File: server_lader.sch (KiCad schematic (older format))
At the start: 20 parts

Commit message: update
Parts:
- removed D? (x2): DIODE, symbol DIODE
- removed U?: LM7909CT, TO-220, symbol LM7909CT
- removed U?: LM7809CT, TO-220, symbol LM7809CT
- added C? (x2): 10nF, symbol C
- added C? (x2): 10uF, symbol C
- added C? (x3): 100nF, symbol C
- added C?: 1uF, symbol C
- added DISP?: EA_DOG-M, symbol EA_DOG-M
- added R?: R1, symbol R
- added R?: R2, symbol R
- added U?: TPS7A4901, symbol TPS7A4901
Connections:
- net labels added: +5VA
- net labels removed: AGND
- wire segments 49 -> 52
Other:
- note added: "DAC8560\nOPA188\n\nADUM3441CRWZ\nRD-0512D"
- note added: "TPS7A4901"
- moved on the sheet: C?, R?, U?A

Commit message: work
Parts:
- removed C? (x2): 1uF, symbol C
- removed R? (x2): 15k, symbol R
- removed U?: LM358, symbol LM358
- added IC?: DAC8560, symbol DAC8560
- added U?: OPA188, symbol TL071
- added U?: RD-0512D, symbol RD-0512D
- added U?: ADUM3441, symbol ADUM3441
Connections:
- net labels added: AGND
- wire segments 52 -> 43
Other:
- note added: "display anschlüsse"
- note removed: "optokoppler"
- moved on the sheet: DISP?, P?

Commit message: bugfixes
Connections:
- wire segments 43 -> 42
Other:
- note removed: "DAC8560\nOPA188\n\nADUM3441CRWZ\nRD-0512D"
- note removed: "TPS7A4901"
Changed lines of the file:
@@
 	1    0    0    -1
 $EndComp
-Text Notes 3400 1600 0    60   ~ 0
-DAC8560\nOPA188\n\nADUM3441CRWZ\nRD-0512D
-Text Notes 7700 950  0    60   ~ 0
-TPS7A4901
 $Comp
 L TPS7A4901 U?
@@
 Wire Wire Line
 	10200 1500 10200 1600
-Wire Wire Line
-	10000 1600 10800 1600
 $Comp
 L C C?
@@
 $EndComp
 Connection ~ 10450 1100
-Wire Wire Line
-	10800 1600 10800 1500
 Connection ~ 10450 1600
 $Comp
@@
 	1    0    0    -1
 $EndComp
+Wire Wire Line
+	10000 1600 10450 1600
+$Comp
+L AGND #PWR?
+U 1 1 5462A127
+P 10800 1500
+F 0 "#PWR?" H 10800 1500 40  0001 C CNN
+F 1 "AGND" H 10800 1430 50  0000 C CNN
+F 2 "" H 10800 1500 60  0000 C CNN
+F 3 "" H 10800 1500 60  0000 C CNN
+	1    10800 1500
+	1    0    0    -1
+$EndComp

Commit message: work
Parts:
- added C?: 1uF, symbol C
- added C? (x2): 100nF, symbol C
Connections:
- wire segments 42 -> 50
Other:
- moved on the sheet: IC?, U?
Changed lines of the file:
@@
 L DAC8560 IC?
 U 1 1 5462BFB9
-P 8950 3400
-F 0 "IC?" H 8950 2900 60  0000 C CNN
-F 1 "DAC8560" H 8950 3400 60  0000 C CNN
-F 2 "" H 7700 2650 60  0000 C CNN
-F 3 "" H 7700 2650 60  0000 C CNN
-	1    8950 3400
+P 9050 3400
+F 0 "IC?" H 9050 2900 60  0000 C CNN
+F 1 "DAC8560" H 9050 3400 60  0000 C CNN
+F 2 "" H 7800 2650 60  0000 C CNN
+F 3 "" H 7800 2650 60  0000 C CNN
+	1    9050 3400
 	1    0    0    -1
 $EndComp
@@
 L ADUM3441 U?
 U 1 1 5462CAA6
-P 7100 3200
-F 0 "U?" H 7400 2600 60  0000 C CNN
-F 1 "ADUM3441" H 7150 3550 60  0000 C CNN
-F 2 "" H 6850 3200 60  0000 C CNN
-F 3 "" H 6850 3200 60  0000 C CNN
-	1    7100 3200
+P 7350 3700
+F 0 "U?" H 7650 3100 60  0000 C CNN
+F 1 "ADUM3441" H 7400 4050 60  0000 C CNN
+F 2 "" H 7100 3700 60  0000 C CNN
+F 3 "" H 7100 3700 60  0000 C CNN
+	1    7350 3700
 	1    0    0    -1
 $EndComp
@@
 	1    0    0    -1
 $EndComp
+Wire Wire Line
+	7900 3700 8300 3700
+Wire Wire Line
+	7900 3800 8300 3800
+Wire Wire Line
+	7900 3900 8300 3900
+$Comp
+L AGND #PWR?
+U 1 1 5462B7A5
+P 7900 4200
+F 0 "#PWR?" H 7900 4200 40  0001 C CNN
+F 1 "AGND" H 7900 4130 50  0000 C CNN
+F 2 "" H 7900 4200 60  0000 C CNN
+F 3 "" H 7900 4200 60  0000 C CNN
+	1    7900 4200
+	0    -1   -1   0
+$EndComp
+$Comp
+L AGND #PWR?
+U 1 1 5462B837
+P 7900 3600
+F 0 "#PWR?" H 7900 3600 40  0001 C CNN
+F 1 "AGND" H 7900 3530 50  0000 C CNN
+F 2 "" H 7900 3600 60  0000 C CNN
+F 3 "" H 7900 3600 60  0000 C CNN
+	1    7900 3600
+	0    -1   -1   0
+$EndComp
+$Comp
+L +5VA #PWR?
+U 1 1 5462B9BC
+P 7900 3500
+F 0 "#PWR?" H 7900 3630 20  0001 C CNN
+F 1 "+5VA" H 7900 3600 30  0000 C CNN
+F 2 "" H 7900 3500 60  0000 C CNN
+F 3 "" H 7900 3500 60  0000 C CNN
+	1    7900 3500
+	1    0    0    -1
+$EndComp
+$Comp
+L VCC #PWR?
+U 1 1 5462BAA9
+P 6850 3500
+F 0 "#PWR?" H 6850 3600 30  0001 C CNN
+F 1 "VCC" H 6850 3600 30  0000 C CNN
+F 2 "" H 6850 3500 60  0000 C CNN
+F 3 "" H 6850 3500 60  0000 C CNN
+	1    6850 3500
+	1    0    0    -1
+$EndComp
+$Comp
+L GND #PWR?
+U 1 1 5462BB3B
+P 6850 3600
+F 0 "#PWR?" H 6850 3600 30  0001 C CNN
+F 1 "GND" H 6850 3530 30  0001 C CNN
+F 2 "" H 6850 3600 60  0000 C CNN
+F 3 "" H 6850 3600 60  0000 C CNN
+	1    6850 3600
+	0    1    1    0
+$EndComp
+$Comp
+L GND #PWR?
+U 1 1 5462BB61
+P 6850 4200
+F 0 "#PWR?" H 6850 4200 30  0001 C CNN
+F 1 "GND" H 6850 4130 30  0001 C CNN
+F 2 "" H 6850 4200 60  0000 C CNN
+F 3 "" H 6850 4200 60  0000 C CNN
+	1    6850 4200
+	0    1    1    0
+$EndComp
+$Comp
+L C C?
+U 1 1 5462C075
+P 7550 2900
+F 0 "C?" H 7550 3000 40  0000 L CNN
+F 1 "1uF" H 7556 2815 40  0000 L CNN
+F 2 "" H 7588 2750 30  0000 C CNN
+F 3 "" H 7550 2900 60  0000 C CNN
+	1    7550 2900
+	1    0    0    -1
+$EndComp
+$Comp
+L C C?
+U 1 1 5462C2DF
+P 8250 3250
+F 0 "C?" H 8250 3350 40  0000 L CNN
+F 1 "100nF" H 8256 3165 40  0000 L CNN
+F 2 "" H 8288 3100 30  0000 C CNN
+F 3 "" H 8250 3250 60  0000 C CNN
+	1    8250 3250
+	1    0    0    -1
+$EndComp
+$Comp
+L C C?
+U 1 1 5462C429
+P 8050 3250
+F 0 "C?" H 8050 3350 40  0000 L CNN
+F 1 "100nF" H 8056 3165 40  0000 L CNN
+F 2 "" H 8088 3100 30  0000 C CNN
+F 3 "" H 8050 3250 60  0000 C CNN
+	1    8050 3250
+	1    0    0    -1
+$EndComp
+Wire Wire Line
+	8050 3050 8300 3050
+$Comp
+L GND #PWR?
+U 1 1 5462C4B3
+P 8250 3450
+F 0 "#PWR?" H 8250 3450 30  0001 C CNN
+F 1 "GND" H 8250 3380 30  0001 C CNN
+F 2 "" H 8250 3450 60  0000 C CNN
+F 3 "" H 8250 3450 60  0000 C CNN
+	1    8250 3450
+	1    0    0    -1
+$EndComp
+$Comp
+L GND #PWR?
+U 1 1 5462C4DC
+P 8050 3450
+F 0 "#PWR?" H 8050 3450 30  0001 C CNN
+F 1 "GND" H 8050 3380 30  0001 C CNN
+F 2 "" H 8050 3450 60  0000 C CNN
+F 3 "" H 8050 3450 60  0000 C CNN
+	1    8050 3450
+	1    0    0    -1
+$EndComp
+$Comp
+L GND #PWR?
+U 1 1 5462C505
+P 7550 3100
+F 0 "#PWR?" H 7550 3100 30  0001 C CNN
+F 1 "GND" H 7550 3030 30  0001 C CNN
+F 2 "" H 7550 3100 60  0000 C CNN
+F 3 "" H 7550 3100 60  0000 C CNN
+	1    7550 3100
+	1    0    0    -1
+$EndComp
+Wire Wire Line
+	7550 2700 7950 2700
+Wire Wire Line
+	7950 2700 7950 2900
+Wire Wire Line
+	7950 2900 8300 2900
+Connection ~ 8250 3050
+$Comp
+L GND #PWR?
+U 1 1 5462C873
+P 9800 3900
+F 0 "#PWR?" H 9800 3900 30  0001 C CNN
+F 1 "GND" H 9800 3830 30  0001 C CNN
+F 2 "" H 9800 3900 60  0000 C CNN
+F 3 "" H 9800 3900 60  0000 C CNN
+	1    9800 3900
+	0    -1   -1   0
+$EndComp
+Wire Wire Line
+	9800 3250 9800 3050
 $EndSCHEMATC

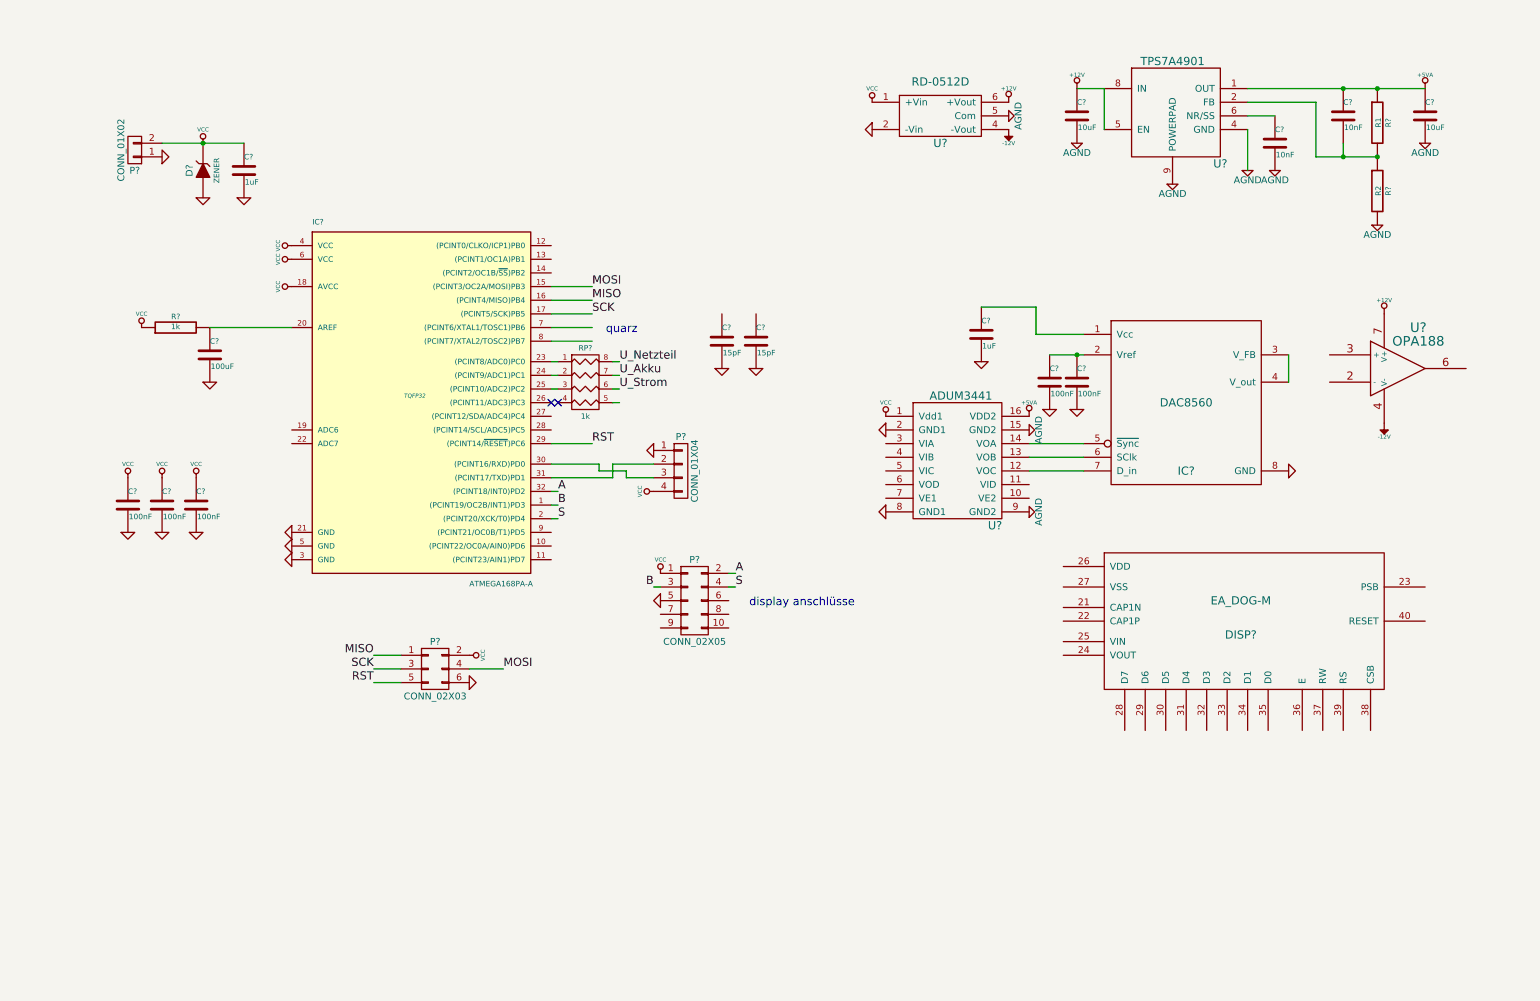
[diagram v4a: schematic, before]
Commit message: app note von TI hinzugefügt
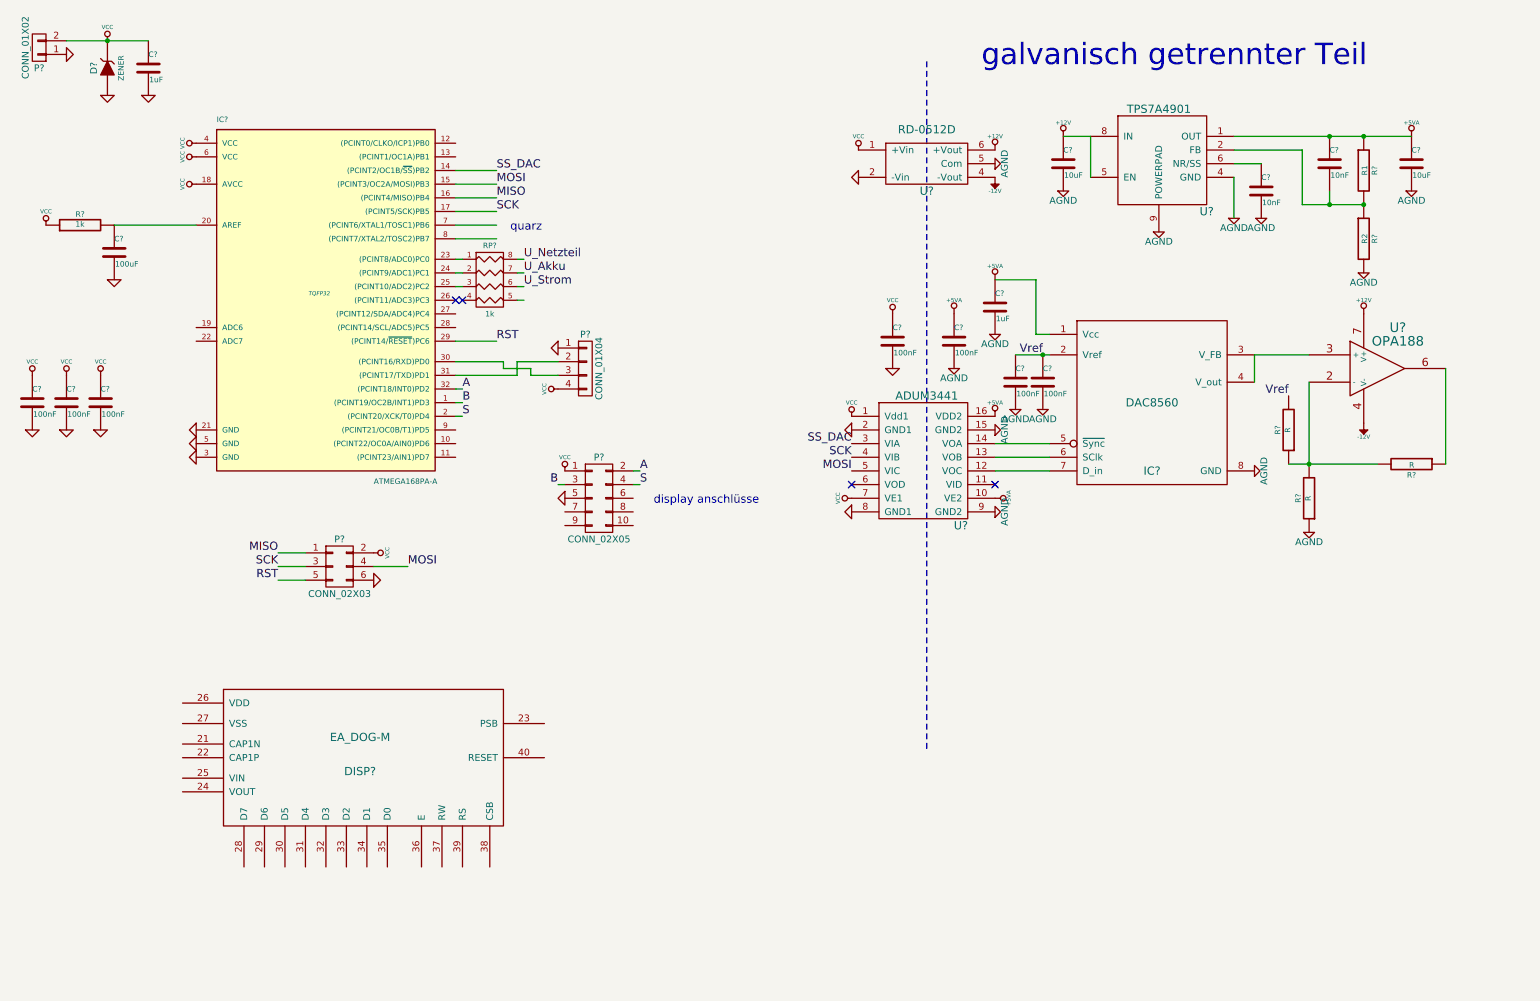
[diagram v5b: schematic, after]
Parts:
- removed C? (x2): 15pF, symbol C
- added C? (x2): 100nF, symbol C
- added R? (x3): R, symbol R
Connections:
- net labels added: SS_DAC, Vref
- wire segments 50 -> 55
- no-connect marks 2 -> 4
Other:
- note added: "galvanisch getrennter Teil"
- moved on the sheet: C?, D?, DISP?, IC?, P?, R?, RP?, U?

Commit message: work Datenblatt hinzugefügt
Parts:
- removed DISP?: EA_DOG-M, symbol EA_DOG-M
- removed P?: CONN_01X02, symbol CONN_01X02
- added C? (x4): 100nF, symbol C
- added C?: C, symbol C
- added C?: 1uF, symbol C
- added DISP?: EA_DOG-M, symbol EA_DOG-M
- added P?: CONN_01X01, symbol CONN_01X01
- added P?: 5V_Vbatt, symbol CONN_01X03
- added P?: IP+, symbol CONN_01X01
- added P?: IP-, symbol CONN_01X01
- added P?: DISPLAY_STECKER, symbol CONN_02X05
- added P?: Drehrad, symbol CONN_01X06
- added P?: on/off, symbol CONN_01X03
- added P?: I2C, symbol CONN_01X03
- added R? (x4): R, symbol R
- added R?: 1k, symbol R
- added R? (x2): 20k, symbol R
- added SP?: SPEAKER, symbol SPEAKER
- added U?: ACS758, symbol ACS758
- added U?: OPTO-TRANSISTOR4, symbol OPTO-TRANSISTOR4
- P?: value CONN_02X05 -> DISPLAY_STECKER
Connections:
- net labels added: +5V, A_D, B_D, CSB, CSB_D, MISO_D, MOSI_D, RS, RS_D, SCK_D, S_D, U_reserve, on
- net labels removed: U_Akku
- wire segments 55 -> 69
- no-connect marks 4 -> 9
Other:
- note added: "CSB=chip select ; equals ss\nactive low; means CSB is low while sending data"
- note added: "Display Platine"
- note added: "RS low: Instruction write operation\nRS high: Data write operation"
- note added: "Resonator"
- note removed: "display anschlüsse"
- note removed: "quarz"
- moved on the sheet: P?

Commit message: work Datenblatt hinzugefügt
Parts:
- removed DISP?: EA_DOG-M, symbol EA_DOG-M
- removed RP?: 1k, symbol R_PACK4
- added C? (x2): 100nF, symbol C
- added C?: C_comp, symbol C
- added D2: LED, symbol LED
- added DISP1: EA_DOG-M, symbol EA_DOG-M
- added F?: FUSE, symbol FUSE
- added P?: on/off, symbol CONN_01X03
- added R2: 200R, symbol R
- added R3: 1k, symbol R
- added R?: R, symbol R
- added X1: Resonator CSTCE16M0V53, symbol CRYSTAL_SMD
- D1: renamed from D?; value ZENER -> ZENER 5,6V
- R11: renamed from R?; value R -> R_G2
- R12: renamed from R?; value R -> R_G1
- R15: renamed from R?; value R -> R_FB
- R6: renamed from R?; value R -> 12k
- R7: renamed from R?; value R -> 1k
- U2: renamed from U?; value OPTO-TRANSISTOR4 -> LTV-356T
- gave numbers to parts that had none: 47
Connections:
- net +12V: now also C?.1
- net -12V: now also C?.2
- net AGND: now also C?.1, C?.2, P?.1 (P1)
- net CSB_D: now also DISP1.38 (CSB)
- net GND: now also D2.2 (K), DISP1.23 (PSB), DISP1.27 (VSS), DISP1.37 (RW), X1.GND
- net MISO_D: now also DISP1.28 (D7)
- net RS_D: now also DISP1.39 (RS)
- net SCK_D: now also DISP1.29 (D6)
- net U_Netzteil: now also IC1.23 ((PCINT8/ADC0)PC0)
- net U_Strom: now also IC1.25 ((PCINT10/ADC2)PC2)
- net U_reserve: now also IC1.24 ((PCINT9/ADC1)PC1)
- net VCC: now also DISP1.24 (VOUT), DISP1.25 (VIN), DISP1.26 (VDD), DISP1.30 (D5), DISP1.31 (D4), DISP1.32 (D3), DISP1.33 (D2), DISP1.34 (D1), DISP1.35 (D0), DISP1.36 (E), DISP1.40 (RESET), F?.2; no longer P1.2 (P2)
- net on: now also R2.1; no longer IC1.12 ((PCINT0/CLKO/ICP1)PB0)
- net at IC1.11 ((PCINT23/AIN1)PD7): now also R?.1; no longer SP1.1
- net at IC1.26 ((PCINT11/ADC3)PC3): now also R3.2
- net at IC1.7 ((PCINT6/XTAL1/TOSC1)PB6): now also X1.2
- net at IC1.8 ((PCINT7/XTAL2/TOSC2)PB7): now also X1.1
- net at R11.1, R12.2, R15.2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: now also C?.2
- net V_current: now reaches R15.1, U6.6
- net V_current: now also C?.1, P?.2 (P2)
- new net: IC1.12 ((PCINT0/CLKO/ICP1)PB0), R2.2
- new net: F?.1, P1.2 (P2)
- new net: R?.2, SP1.1
- new net: D2.1 (A), R3.1
- no-connect marks 9 -> 8
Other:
- note removed: "Resonator"
- moved on the sheet: C5, D1, R15, SP1

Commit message: work
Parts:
- removed P4: I2C, symbol CONN_01X03
- added C?: 1uF, symbol C
- added P4: I2C, Sockets_MOLEX_KK-System:Socket_MOLEX-KK-RM2-54mm_Lock_4pin_straight, symbol CONN_01X04
- added R?: 10k, symbol R
- C1, C12, C13, C15, C16, C18, C19, C2, C3, C4, C6, C7, C8, C9: footprint (none) -> SMD_Packages:SMD-0402
- C10, C14, C5, D2: footprint (none) -> SMD_Packages:SMD-0603
- C11: value C -> 100nF; footprint (none) -> SMD_Packages:SMD-0402
- C17: footprint (none) -> SMD_Packages:SMD-1206
- C20: renamed from C?; footprint (none) -> SMD_Packages:SMD-0603
- C21: renamed from C20; footprint (none) -> SMD_Packages:SMD-1206
- C22, C23: renamed from C?; footprint (none) -> SMD_Packages:SMD-0402
- DISP1: footprint (none) -> toni:EA_DOG-M_DISP
- F1: renamed from F?; footprint (none) -> toni:fuse_holder_Schurther
- IC1: footprint TQFP32 -> SMD_Packages:TQFP-32
- IC2: footprint (none) -> Housings_SSOP:MSOP-8_3x3mm_Pitch0.65mm
- P1, P11: footprint (none) -> Sockets_MOLEX_KK-System:Socket_MOLEX-KK-RM2-54mm_Lock_3pin_straight
- P12: renamed from P?; value on/off -> A_regulation_out; footprint (none) -> Sockets_MOLEX_KK-System:Socket_MOLEX-KK-RM2-54mm_Lock_3pin_straight
- P3: footprint (none) -> toni:micro_match3x2
- P7: value CONN_01X04 -> UART; footprint (none) -> Sockets_MOLEX_KK-System:Socket_MOLEX-KK-RM2-54mm_Lock_4pin_straight
- P9: footprint (none) -> Sockets_MOLEX_KK-System:Socket_MOLEX-KK-RM2-54mm_Lock_6pin_straight
- R1, R2, R4, R5: footprint (none) -> SMD_Packages:SMD-0805
- R10: renamed from R9; footprint (none) -> SMD_Packages:SMD-0805
- R11: renamed from R10; footprint (none) -> SMD_Packages:SMD-0805
- R12: renamed from R11; footprint (none) -> SMD_Packages:SMD-0805
- R13: renamed from R12; footprint (none) -> SMD_Packages:SMD-0805
- R14: renamed from R13; footprint (none) -> SMD_Packages:SMD-0805
- R15: renamed from R14; footprint (none) -> SMD_Packages:SMD-0805
- R16: renamed from R15; footprint (none) -> SMD_Packages:SMD-0805
- R3: renamed from R?; footprint (none) -> SMD_Packages:SMD-0805
- R6: renamed from R3; footprint (none) -> SMD_Packages:SMD-0805
- R7: renamed from R6; footprint (none) -> SMD_Packages:SMD-0805
- R8: renamed from R7; footprint (none) -> SMD_Packages:SMD-0805
- R9: renamed from R8; footprint (none) -> SMD_Packages:SMD-0805
- SP1: footprint (none) -> toni:Buzzer_AI-1027-TWT-5V-R
- U2: footprint (none) -> toni:SO-4
- U3: footprint (none) -> Housings_SOIC:SOIC-16_7.5x10.3mm_Pitch1.27mm
- U5: footprint (none) -> toni:MSOP-8_power_pad
- U6: footprint (none) -> SMD_Packages:SSOP-8
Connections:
- net GND: now also C?.2, P4.1 (P1)
- net MISO_D: no longer DISP1.28 (D7)
- net MOSI_D: now also DISP1.28 (D7)
- net U_Strom: now also C?.1, R?.1; no longer U1.3 (VIOUT)
- net VCC: now also P4.4 (P4)
- net at IC1.27 ((PCINT12/SDA/ADC4)PC4): now also P4.3 (P3)
- net at IC1.28 ((PCINT14/SCL/ADC5)PC5): now also P4.2 (P2)
- new net: R?.2, U1.3 (VIOUT)
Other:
- moved on the sheet: C11, D2, R6
